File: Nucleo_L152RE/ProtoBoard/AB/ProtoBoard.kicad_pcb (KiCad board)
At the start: 2 copper layers, 68.6 x 119.5 mm, 159 parts, among them CON1 USB-MICRO-B, J1 EXTPower, J2 EXT, P1 Hole, P10 GND, P11 GND, P12 GND, P13 GND, P14 GND, P15 GND, P16 GND, P17 GND, P18 GND, P19 3.3Ctl, P2 Hole, P20 3.3Ctl, P21 3.3Ctl, P22 3.3V, P23 3.3V, P24 3.3V, P25 5.0V, P26 5.0V, P27 5.0V, P28 Servo, P29 Servo, P3 Hole, P30 Servo, P31 Power2, P32 SWBUS1, P33 VinPower, P34 ServoPower, P35 Power1, P36 USART2, P37 SWD Header, P38 RGB1, P39 USART1, P4 Hole, P40 MS1, P41 MS3, P42 MS2, P43 MS4, P44 WS1, P45 OW1_A, P46 I2C1_A, P47 I2C2_A, P48 WS2, P49 I2C1_B, P5 GND1, P50 I2C2_B, P52 WS3, P53 OW2_A, P54 OW3_A, P55 Ant, P6 GND2, P7 GND, P8 GND, P9 GND, SW1 MomentarySwitch, SW2 ResetSwitch, U1 LDS3985, U2 Nucleo-L152RE-CN7, U3 Nucleo-L152RE-CN10, U4 S25FL127S, U5 MT3329_GPS, U6 RFM69HW, U7 ATSHA204A

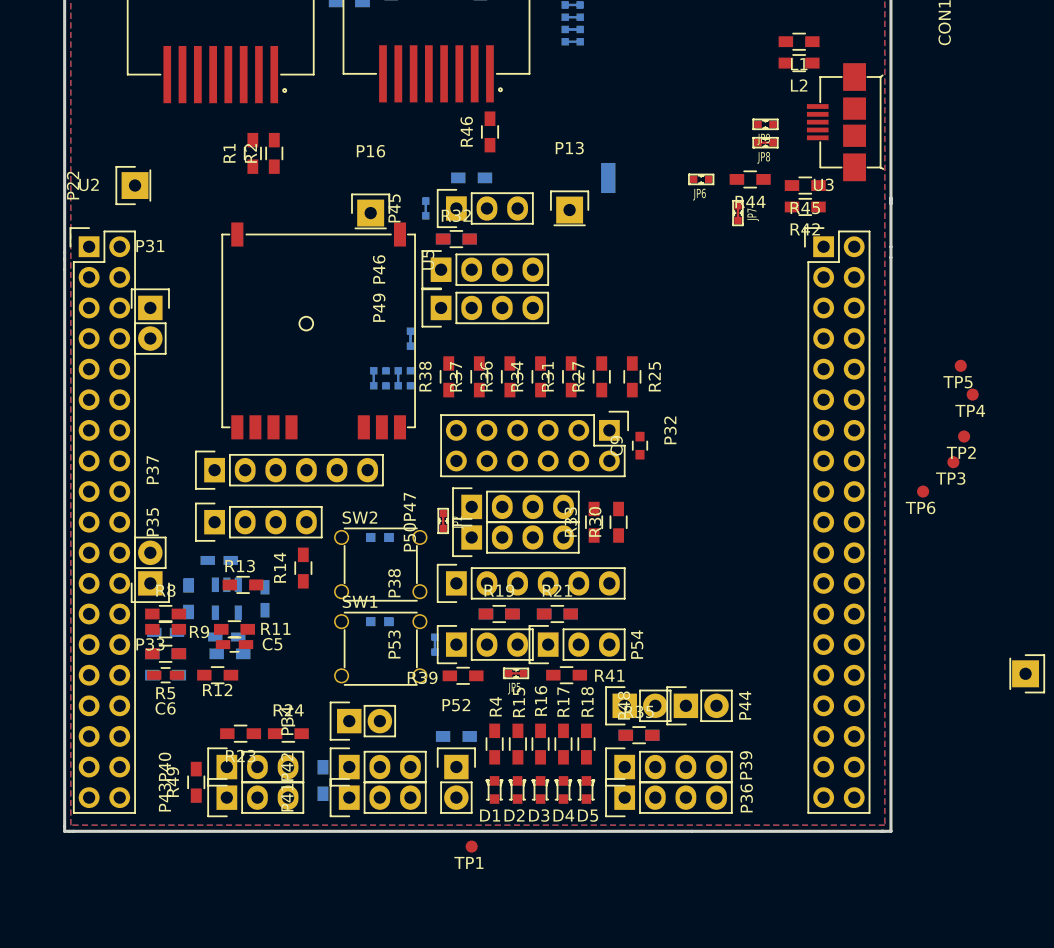
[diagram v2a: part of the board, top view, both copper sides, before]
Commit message: One of the connectors is routed, now to do the other one.
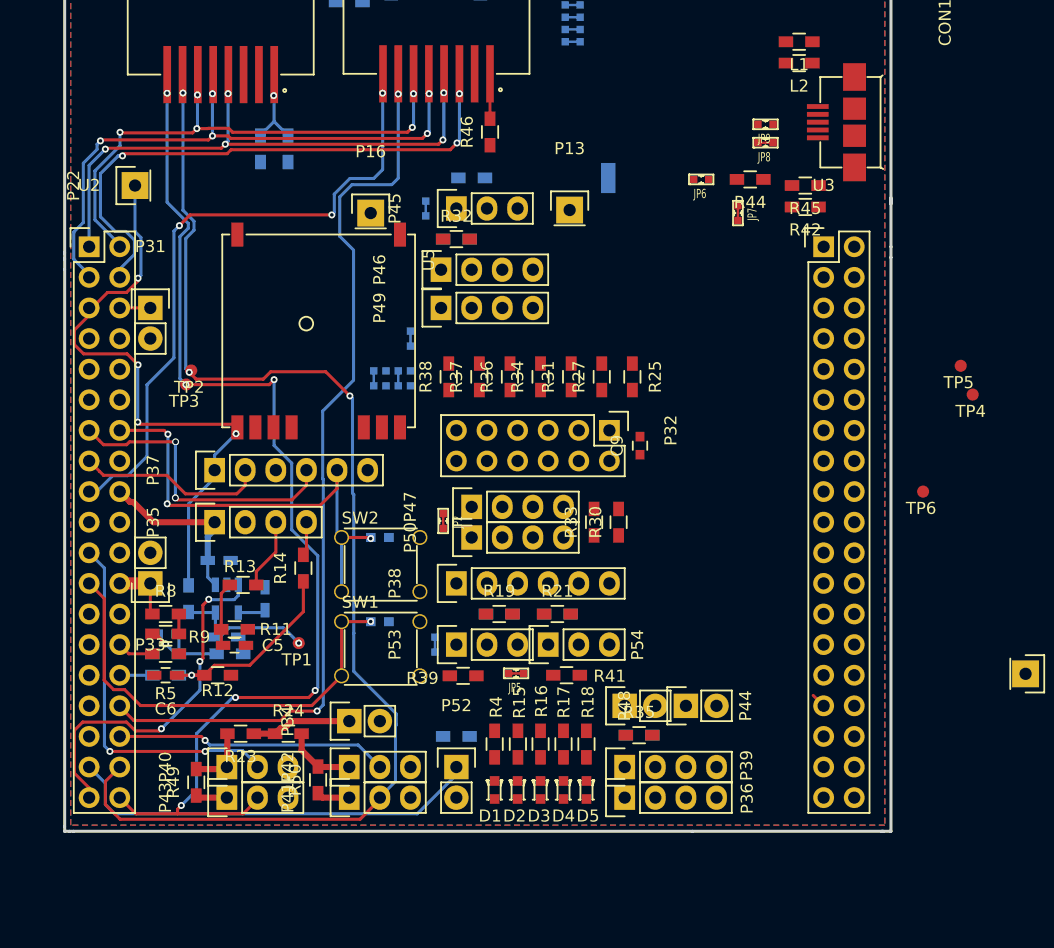
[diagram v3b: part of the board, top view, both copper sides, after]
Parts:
- R1, R2: moved to B.Cu
- R50: moved to F.Cu
- moved TP2 64.4 mm to (132.9, 90.3)
- moved TP3 64.0 mm to (132.5, 91.4)
- moved TP1 22.2 mm to (141.9, 112.9)
- moved R1 2.95 mm to (141.0, 71.9)
- moved R2 1.20 mm to (138.7, 71.9)
- moved R50 0.41 mm to (143.5, 124.3)
- moved R9 0.38 mm to (130.8, 112.1)
- moved C4 0.18 mm to (130.9, 112.1), turned to 0 degrees
- moved C5 0.06 mm to (136.5, 113.1)
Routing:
- net MotionSense3: track 0.00 -> 103.4 mm, vias 0 -> 3
- net MotionSense4: track 0.00 -> 93.1 mm, vias 0 -> 6
- net EXT_ADC: track 0.00 -> 75.8 mm, vias 0 -> 2
- net EXT_GPIO: track 0.00 -> 55.6 mm, vias 0 -> 3
- net EXT_SPI_MOSI: track 0.00 -> 52.0 mm, vias 0 -> 5
- net EXT_SPI_SCK: track 0.00 -> 51.6 mm, vias 0 -> 5
- net +3V3: track 0.00 -> 50.7 mm, vias 0 -> 4
- net EXT_SPI_CS: track 0.00 -> 47.3 mm, vias 0 -> 3
- net EXT_SPI_MISO: track 0.00 -> 45.0 mm, vias 0 -> 5
- net NRST: track 0.00 -> 39.6 mm, vias 0 -> 3
- net StatusButton1: track 0.00 -> 37.1 mm, vias 0 -> 1
- net WS3: track 0.00 -> 35.1 mm
- net MotionSense1: track 0.00 -> 30.2 mm, vias 0 -> 2
- net SensorVEnable: track 0.00 -> 29.8 mm, vias 0 -> 3
- net TMS: track 0.00 -> 25.1 mm, vias 0 -> 2
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
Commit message: Added many traces which will have to be removed since I put via's on pads :/
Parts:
- JP1, JP10, JP12, JP14, JP15, JP16, JP17, JP2, JP3, JP4, JP5, JP7, JP8: footprint nucleo:SB_NC_Smaller -> nucleo:SB_NO_Smaller
- JP9: value Jumper_NO_Small -> Jumper_Small
- R26: moved to F.Cu
- moved R35 6.99 mm to (175.3, 115.8)
- moved R26 4.73 mm to (170.2, 115.8), turned to 180 degrees
- moved R47 3.12 mm to (164.0, 58.1)
- moved JP17 0.25 mm to (164.6, 59.7)
- moved JP14 0.13 mm to (164.6, 63.1)
- moved JP16 0.13 mm to (164.6, 60.8)
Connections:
- CON1 pad 4: Net-(CON1-Pad4) -> StatusLed2
- JP1 pad 2: Net-(JP1-Pad2) -> 3.3Vctl
- JP10 pad 2: Net-(JP10-Pad2) -> I2C_SDA2
- JP11 pad 2: Net-(JP10-Pad2) -> I2C_SDA2
- JP12 pad 2: Net-(JP12-Pad2) -> I2C_SCL2
- JP13 pad 2: Net-(JP12-Pad2) -> I2C_SCL2
- JP14 pad 1: Net-(JP14-Pad1) -> SPI2_NSS
- JP15 pad 1: Net-(JP15-Pad1) -> SPI2_MOSI
- JP16 pad 1: Net-(JP16-Pad1) -> SPI2_MISO
- JP17 pad 1: Net-(JP17-Pad1) -> SPI2_SCK
- JP2 pad 2: Net-(JP2-Pad2) -> 3.3Vctl
- JP3 pad 2: Net-(JP3-Pad2) -> 3.3Vctl
- JP4 pad 2: Net-(JP4-Pad2) -> 3.3Vctl
- JP5 pad 2: Net-(JP5-Pad2) -> 3.3Vctl
- JP6 pad 2: Net-(JP6-Pad2) -> U5V
- JP7 pad 2: Net-(JP6-Pad2) -> U5V
- JP8 pad 2: Net-(CON1-Pad4) -> StatusLed2
- JP9 pad 2: Net-(CON1-Pad4) -> StatusLed2
- P45 pad 1: Net-(JP3-Pad2) -> 3.3Vctl
- P46 pad 1: Net-(JP1-Pad2) -> 3.3Vctl
- P47 pad 1: Net-(JP2-Pad2) -> 3.3Vctl
- P49 pad 1: Net-(JP1-Pad2) -> 3.3Vctl
- P50 pad 1: Net-(JP2-Pad2) -> 3.3Vctl
- P53 pad 1: Net-(JP4-Pad2) -> 3.3Vctl
- P54 pad 1: Net-(JP5-Pad2) -> 3.3Vctl
- R28 pad 2: Net-(JP3-Pad2) -> 3.3Vctl
- R29 pad 1: Net-(JP1-Pad2) -> 3.3Vctl
- R30 pad 1: Net-(JP2-Pad2) -> 3.3Vctl
- R32 pad 1: Net-(JP1-Pad2) -> 3.3Vctl
- R33 pad 1: Net-(JP2-Pad2) -> 3.3Vctl
- R39 pad 2: Net-(JP4-Pad2) -> 3.3Vctl
- R41 pad 2: Net-(JP5-Pad2) -> 3.3Vctl
- R44 pad 2: Net-(JP6-Pad2) -> U5V
- U5 pad 10: Net-(JP12-Pad2) -> I2C_SCL2
- U5 pad 9: Net-(JP10-Pad2) -> I2C_SDA2
- U6 pad 12: Net-(JP17-Pad1) -> SPI2_SCK
- U6 pad 13: Net-(JP16-Pad1) -> SPI2_MISO
- U6 pad 14: Net-(JP15-Pad1) -> SPI2_MOSI
- U6 pad 15: Net-(JP14-Pad1) -> SPI2_NSS
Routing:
- net SPI2_SCK: track 0.00 -> 103.5 mm, vias 0 -> 7
- net SPI2_MISO: track 0.00 -> 98.4 mm, vias 0 -> 5
- net StatusLed2: track 0.00 -> 86.7 mm, vias 0 -> 4
- net SWO: track 1.22 -> 60.0 mm, vias 0 -> 2
- net USART1_TX: track 0.00 -> 56.1 mm, vias 0 -> 3
- net USART2_TX: track 0.00 -> 19.8 mm
- net WS2: track 0.00 -> 18.2 mm, vias 0 -> 3
- net USART2_RX: track 0.00 -> 12.9 mm
- net USART1_RX: track 0.00 -> 12.6 mm
- net I2C_SDA2: track 0.00 -> 6.48 mm, vias 0 -> 1
- net I2C_SCL2: track 0.00 -> 6.07 mm, vias 0 -> 1
- net 3.3Vctl: track 5.36 -> 9.08 mm
- net WS3: track 35.1 -> 38.1 mm
- net SPI2_NSS: track 0.00 -> 1.24 mm
- net SPI2_MOSI: track 0.00 -> 1.24 mm

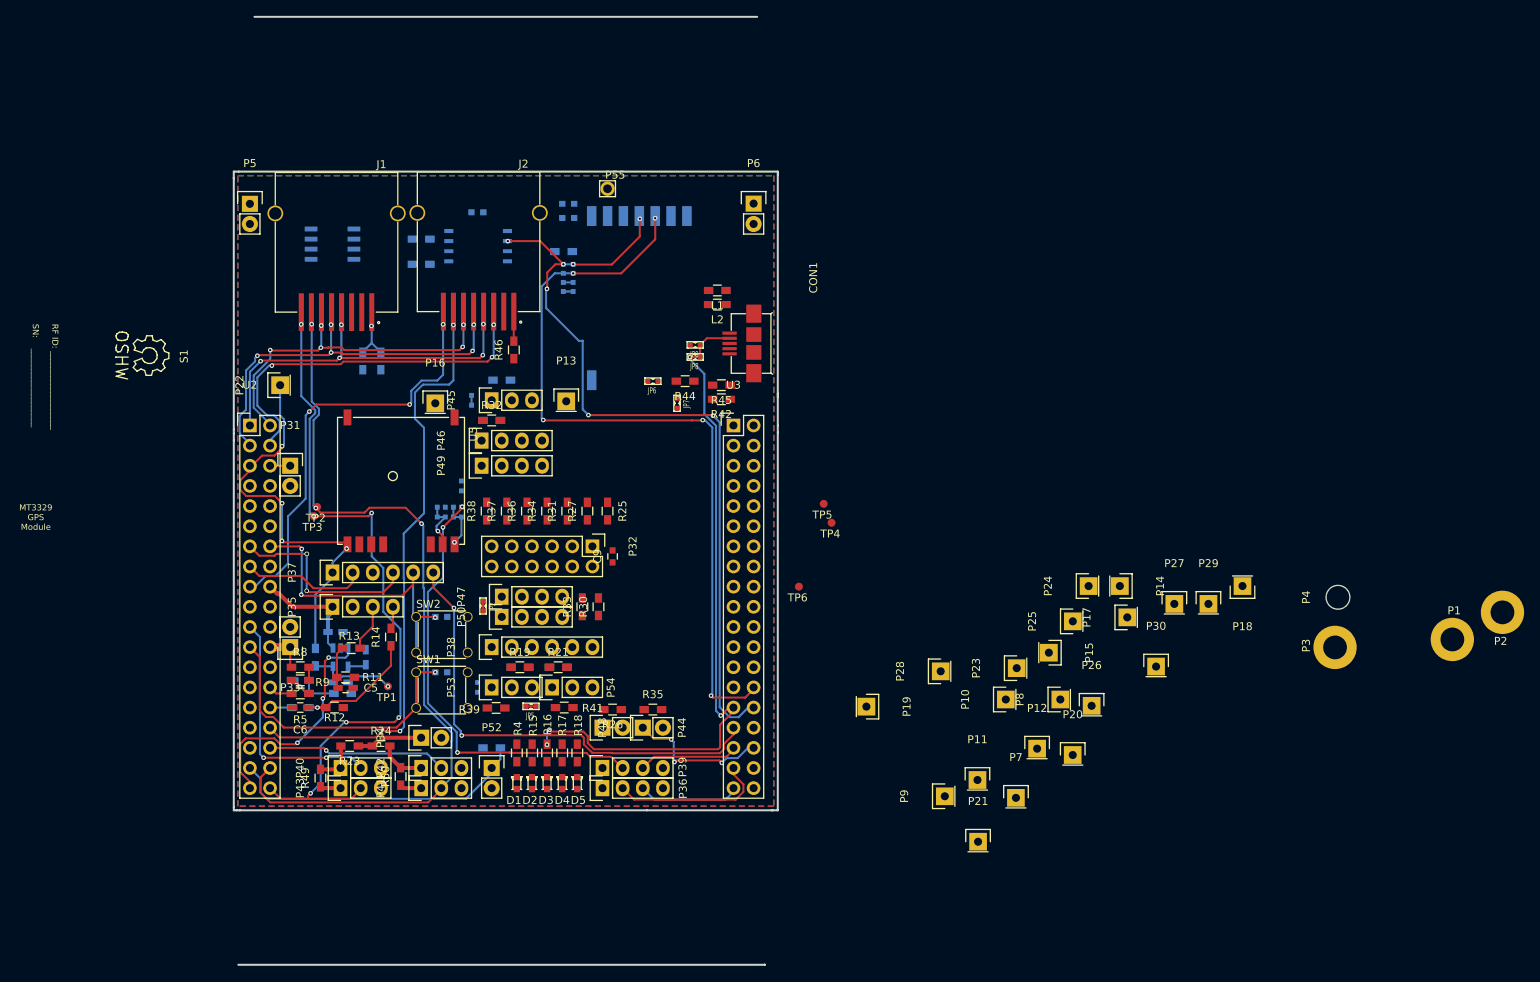
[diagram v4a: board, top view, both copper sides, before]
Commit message: Final draft with all traces and artwork in place.
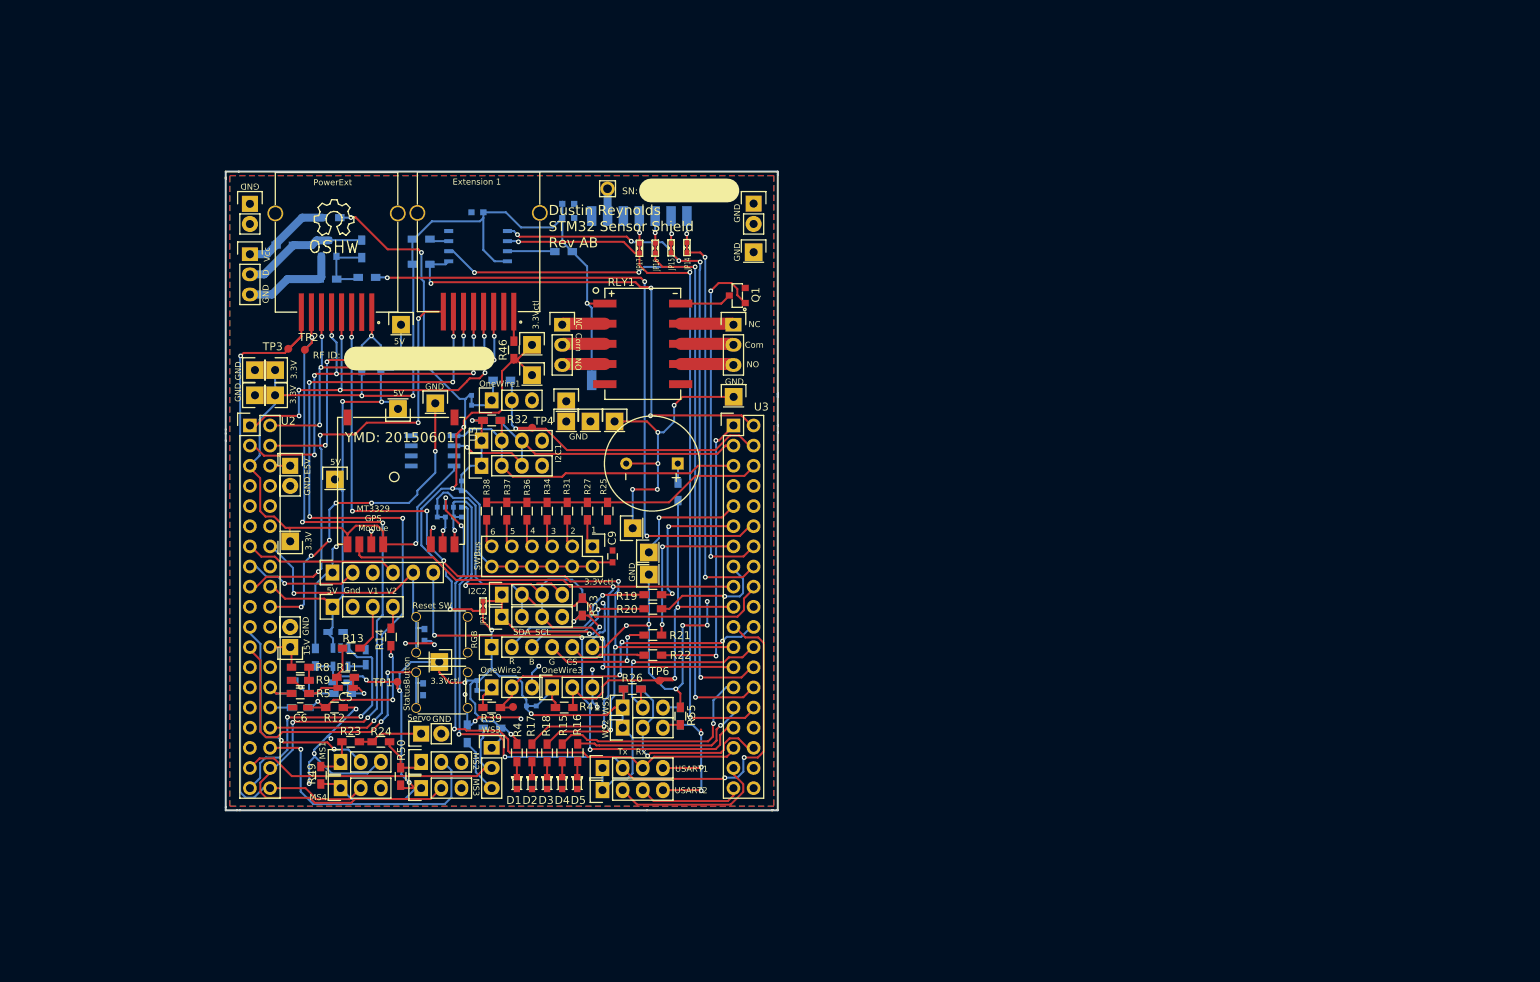
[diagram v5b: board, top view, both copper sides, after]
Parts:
- removed CON1: USB-MICRO-B, nucleo:USB_micro_AB
- removed JP6: Jumper_NO_Small, nucleo:SB_NO_Smaller
- removed JP7, JP8: Jumper_NC_Small, nucleo:SB_NO_Smaller
- removed JP9: Jumper_Small, nucleo:SB_NO_Smaller
- removed L1, L2: 600 Ohm, Resistors_SMD:R_0603_HandSoldering
- removed P1, P2, P3: Hole, nucleo:plat_hole_4_20
- removed P28, P29, P30: Servo, Pin_Headers:Pin_Header_Straight_1x01
- removed P4: Hole, Mounting_Holes:MountingHole_3mm
- added B1: Piezo, nucleo:Piezo_12mm, F.Cu at (175.1, 84.8)
- added P51: FET_SW1, Pin_Headers:Pin_Header_Straight_1x03, F.Cu at (124.5, 58.4)
- added P56: WS2, Pin_Headers:Pin_Header_Straight_1x03, F.Cu at (171.4, 118.1)
- added P57: WS2, Pin_Headers:Pin_Header_Straight_1x03, F.Cu at (154.9, 120.7)
- added Q1: BSS123-7-F, nucleo:SOT23-3, F.Cu at (185.9, 63.6)
- added Q2: BSS123-7-F, nucleo:SOT23-3, B.Cu at (134.4, 57.7)
- added R51: 220, Resistors_SMD:R_0603_HandSoldering, B.Cu at (178.4, 88.4)
- added R52: 0, Resistors_SMD:R_0603_HandSoldering, B.Cu at (128.9, 57.3)
- added R53: 0, Resistors_SMD:R_0603_HandSoldering, B.Cu at (134.7, 53.8)
- added R54: 0, Resistors_SMD:R_0603_HandSoldering, B.Cu at (178.7, 116.6)
- added R55: 0, Resistors_SMD:R_0603_HandSoldering, F.Cu at (178.7, 116.6)
- added R56: 0, Resistors_SMD:R_0603_HandSoldering, B.Cu at (151.9, 118.9)
- added RLY1: TQ2SA-3V, nucleo:Relay_SMD, F.Cu at (174.0, 69.7)
- D2: value Red -> Green
- D3: value Yellow -> Blue
- D4: value Green -> Red
- D5: value Blue -> Yellow
- JP14, JP15, JP16, JP17, R20, R22: moved to F.Cu
- JP5, R30, R35, R44: moved to B.Cu
- P44: value WS1 -> RLY1; footprint Pin_Headers:Pin_Header_Straight_1x02 -> Pin_Headers:Pin_Header_Straight_1x03
- P48: value WS2 -> RLY2; footprint Pin_Headers:Pin_Header_Straight_1x02 -> Pin_Headers:Pin_Header_Straight_1x03
- P52: value WS3 -> WS1; footprint Pin_Headers:Pin_Header_Straight_1x02 -> Pin_Headers:Pin_Header_Straight_1x03
- R42, R45: value 33 -> 0; moved to B.Cu
- moved P18 127.4 mm to (125.1, 73.0), turned to 90 degrees
- moved P14 111.7 mm to (125.1, 76.2), turned to 90 degrees
- moved P27 107.0 mm to (135.2, 86.8)
- moved P24 100.8 mm to (129.5, 94.6), turned to 180 degrees
- moved P23 100.8 mm to (127.6, 73.0), turned to 270 degrees
- moved P26 99.4 mm to (143.5, 67.3)
- moved P25 89.2 mm to (143.1, 77.9), turned to 180 degrees
- moved P21 84.2 mm to (160.0, 69.8)
- moved P20 83.3 mm to (160.0, 73.7)
- moved P12 72.3 mm to (164.3, 79.5)
- moved P17 69.2 mm to (170.4, 79.5), turned to 0 degrees
- moved P8 68.4 mm to (188.0, 58.2), turned to 0 degrees
- moved P15 64.7 mm to (167.4, 79.5), turned to 0 degrees
- moved P7 61.8 mm to (185.4, 76.4)
- moved P19 54.1 mm to (148.3, 109.8)
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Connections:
- C3 pad 2: 3.3Ctl -> 3.3Vctl
- P19 pad 1: 3.3Ctl -> 3.3Vctl
- P20 pad 1: 3.3Ctl -> 3.3Vctl
- P21 pad 1: 3.3Ctl -> 3.3Vctl
- P44 pad 1: WS1 -> Net-(P44-Pad1)
- P44 pad 2: GND -> Net-(P44-Pad2)
- P48 pad 1: WS2 -> Net-(P48-Pad1)
- P48 pad 2: GND -> Net-(P48-Pad2)
- P52 pad 1: WS3 -> 3.3Vctl
- P52 pad 2: GND -> WS1
- R15 pad 2: Net-(D2-Pad2) -> Net-(D4-Pad2)
- R16 pad 2: Net-(D3-Pad2) -> Net-(D5-Pad2)
- R17 pad 2: Net-(D4-Pad2) -> Net-(D2-Pad2)
- R18 pad 2: Net-(D5-Pad2) -> Net-(D3-Pad2)
- R3 pad 2: 3.3Ctl -> 3.3Vctl
- R4 pad 2: 3.3Ctl -> 3.3Vctl
- R42 pad 1: USB_DP -> Net-(Q2-Pad1)
- R42 pad 2: Net-(CON1-Pad3) -> USB_DP
- R44 pad 2: U5V -> Net-(Q2-Pad1)
- R45 pad 1: USB_DM -> Net-(Q2-Pad1)
- R45 pad 2: Net-(CON1-Pad2) -> GND
- TP1 pad 1: 3.3Ctl -> 3.3Vctl
- U1 pad 5: 3.3Ctl -> 3.3Vctl
- U3 pad 8: U5V -> (no net)
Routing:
- net 3.3Vctl: track 9.08 -> 305.3 mm, vias 0 -> 16
- net GND: track 0.00 -> 237.8 mm, vias 0 -> 36
- net +3V3: track 50.7 -> 170.6 mm, vias 4 -> 6
- net StatusLed4: track 0.00 -> 107.6 mm, vias 0 -> 7
- net SPI2_MOSI: track 1.24 -> 92.0 mm, vias 0 -> 6
- net USB_DP: track 0.00 -> 80.3 mm, vias 0 -> 3
- net StatusLed3: track 0.00 -> 78.4 mm, vias 0 -> 2
- net I2C_SCL2: track 6.07 -> 69.9 mm, vias 1 -> 4
- net StatusLed2: track 86.7 -> 23.0 mm, vias 4 -> 1
- net FLASH_nCS: track 0.00 -> 62.8 mm, vias 0 -> 3
- net I2C_SDA2: track 6.48 -> 65.5 mm
- net USART1_RX: track 12.6 -> 71.1 mm, vias 0 -> 3
- net SPI2_NSS: track 1.24 -> 54.2 mm, vias 0 -> 3
- net OneWireBus3: track 0.00 -> 52.5 mm, vias 0 -> 2
- net 5V: track 14.6 -> 62.0 mm, vias 0 -> 2
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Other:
- board size 68.6 x 119.5 mm -> 69.6 x 80.5 mm
- net class Default: via_dia 0.5842 -> 0.6096; via_drill 0.381 -> 0.3048
- net class Power: via_dia 0.5842 -> 0.6096; via_drill 0.381 -> 0.3048
- rule trace_min: 0.1778 -> 0.254
- rule via_min_drill: 0.381 -> 0.3048
- rule via_min_size: 0.5842 -> 0.6096
- board text added: "1"
- board text added: "15V"
- board text added: "2"
- board text added: "3"
- board text added: "3.3V"
- board text added: "3.3Vctl"
- board text added: "4"
- board text added: "5"
- board text added: "5V"
- board text added: "6"
- board text added: "B"
- board text added: "CS"
- board text added: "Com"
- board text added: "D"
- board text added: "Dustin Reynolds STM32 Sensor Shield Rev AB"
- board text added: "E5V"
- board text added: "Ext Bus Pin Out 1. 3.3v 2. Gnd 3. SPI CS 4. SPI CLK 5. SPI MOSI 6. SPI MISO 7. ADC (3.3V only) 8. GPIO/DAC"
- board text added: "Ext Power Connection 1. 5V/3.3V 2. GND 3. StatusLed4 4. SPI CLK 5. SPI MOSI 6. SPI MISO 7. MotionSense3 8. MotionSense4"
- board text added: "G"
- board text added: "GND"
- board text added: "Gnd"
- board text added: "I2C1"
- board text added: "I2C2"
- board text added: "MS1"
- board text added: "MS2"
- board text added: "MS3"
- board text added: "MS4"
- board text added: "NC"
- board text added: "NO"
- board text added: "OneWire1"
- board text added: "OneWire2"
- board text added: "OneWire3"
- board text added: "R"
- board text added: "RF ID:"
- board text added: "RGB"
- board text added: "Reset SW"
- board text added: "Rx"
- board text added: "SCL"
- board text added: "SDA"
- board text added: "SN:"
- board text added: "SWBus"
- board text added: "Servo"
- board text added: "StatusButton"
- board text added: "Tx"
- board text added: "USART1"
- board text added: "USART2"
- board text added: "V1"
- board text added: "V2"
- board text added: "Vcc"
- board text added: "WS1"
- board text added: "WS2"
- board text added: "WS3"
- board text added: "YMD: 20150601"
- board text removed: "Dustin Reynolds STM32 Sensor Shield Nucleo-L152RE"
- board text removed: "Ext Bus Pin Out 1. 3.3v 2. Gnd 3. SPI CS 4. SPI CLK 5. SPI MOSI 6. SPI MISO 7. ADC 8. GPIO/DAC (3.3V only)"
- board text removed: "Ext Power Connection 1. MotionSense3 2. MotionSense4 3. StatusLed4 4. SPI CLK 5. SPI MOSI 6. SPI MISO 7. E5V 8. Gnd"
- board text removed: "RF ID: ___________________ SN: ___________________"
- board text removed: "YMD: 20150410"

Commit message: Finished AB board.
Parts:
- moved D2 3.81 mm to (163.8, 125.1)
- moved D3 3.81 mm to (165.7, 125.1)
- moved D4 3.81 mm to (160.0, 125.1)
- moved D5 3.81 mm to (161.9, 125.1)
- moved R52 2.39 mm to (128.4, 59.6), turned to 90 degrees
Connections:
- R15 pad 2: Net-(D4-Pad2) -> Net-(D2-Pad2)
- R16 pad 2: Net-(D5-Pad2) -> Net-(D3-Pad2)
- R17 pad 2: Net-(D2-Pad2) -> Net-(D4-Pad2)
- R18 pad 2: Net-(D3-Pad2) -> Net-(D5-Pad2)
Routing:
- net GND: track 237.8 -> 225.2 mm
- net Net-(P51-Pad2): track 15.9 -> 16.9 mm
- net Net-(P51-Pad1): track 11.2 -> 12.2 mm
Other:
- board text added: "3.3V ctl"
- board text added: "3.5 to 5.5V"
- board text added: "4.4V Max"
- board text added: "5V:3.5 to 5.5V"
- board text added: "Designed by Dustin Reynolds, June 1, 2015"
- board text added: "E5V:3.5 to 5.5V"
- board text added: "Relay 30V 1A Max"
- board text added: "ST-Link"
- board text added: "Servo: 10V Max"
- board text added: "Stat Led1"
- board text added: "Stat Led2"
- board text added: "Stat Led3"
- board text added: "Stat Led4"
- board text added: "USART2 Connected to ST-Link by default"
- board text added: "Vin 6.5 to 15V"
- board text added: "Website: https://mecharobotics.wordpress.com"
